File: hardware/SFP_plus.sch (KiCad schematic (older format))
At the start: 20 parts, among them U501 SFPP_CONN

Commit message: Layouted USB-UART.
Also moved USB-OTG to the right Side of the Board. To get there
some free Space, i moved the DDR3/Memory and the FPGA a few
Millimeters down.
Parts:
- R501, R502, R503, R504, R505, R506, R507, R508, R509, R510, R511: footprint Resistors_SMD:R_0402 -> Resistor_SMD:R_0402_1005Metric
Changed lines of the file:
@@
 F 0 "R501" V 6880 3050 50  0000 C CNN
 F 1 "10k" V 6800 3050 50  0000 C CNN
-F 2 "Resistors_SMD:R_0402" V 6730 3050 50  0001 C CNN
+F 2 "Resistor_SMD:R_0402_1005Metric" V 6730 3050 50  0001 C CNN
 F 3 "" H 6800 3050 50  0000 C CNN
 	1    6800 3050
@@
 F 0 "R503" V 7080 3050 50  0000 C CNN
 F 1 "10k" V 7000 3050 50  0000 C CNN
-F 2 "Resistors_SMD:R_0402" V 6930 3050 50  0001 C CNN
+F 2 "Resistor_SMD:R_0402_1005Metric" V 6930 3050 50  0001 C CNN
 F 3 "" H 7000 3050 50  0000 C CNN
 	1    7000 3050
@@
 F 0 "R504" V 7280 3050 50  0000 C CNN
 F 1 "10k" V 7200 3050 50  0000 C CNN
-F 2 "Resistors_SMD:R_0402" V 7130 3050 50  0001 C CNN
+F 2 "Resistor_SMD:R_0402_1005Metric" V 7130 3050 50  0001 C CNN
 F 3 "" H 7200 3050 50  0000 C CNN
 	1    7200 3050
@@
 F 0 "R506" V 7480 3050 50  0000 C CNN
 F 1 "10k" V 7400 3050 50  0000 C CNN
-F 2 "Resistors_SMD:R_0402" V 7330 3050 50  0001 C CNN
+F 2 "Resistor_SMD:R_0402_1005Metric" V 7330 3050 50  0001 C CNN
 F 3 "" H 7400 3050 50  0000 C CNN
 	1    7400 3050
@@
 F 0 "R507" V 7680 3050 50  0000 C CNN
 F 1 "10k" V 7600 3050 50  0000 C CNN
-F 2 "Resistors_SMD:R_0402" V 7530 3050 50  0001 C CNN
+F 2 "Resistor_SMD:R_0402_1005Metric" V 7530 3050 50  0001 C CNN
 F 3 "" H 7600 3050 50  0000 C CNN
 	1    7600 3050
@@
 F 0 "R508" V 7880 3050 50  0000 C CNN
 F 1 "10k" V 7800 3050 50  0000 C CNN
-F 2 "Resistors_SMD:R_0402" V 7730 3050 50  0001 C CNN
+F 2 "Resistor_SMD:R_0402_1005Metric" V 7730 3050 50  0001 C CNN
 F 3 "" H 7800 3050 50  0000 C CNN
 	1    7800 3050
@@
 F 0 "R509" V 8080 3050 50  0000 C CNN
 F 1 "10k" V 8000 3050 50  0000 C CNN
-F 2 "Resistors_SMD:R_0402" V 7930 3050 50  0001 C CNN
+F 2 "Resistor_SMD:R_0402_1005Metric" V 7930 3050 50  0001 C CNN
 F 3 "" H 8000 3050 50  0000 C CNN
 	1    8000 3050
@@
 F 0 "R510" V 8380 3450 50  0000 C CNN
 F 1 "1k" V 8300 3450 50  0000 C CNN
-F 2 "Resistors_SMD:R_0402" V 8230 3450 50  0001 C CNN
+F 2 "Resistor_SMD:R_0402_1005Metric" V 8230 3450 50  0001 C CNN
 F 3 "" H 8300 3450 50  0000 C CNN
 	1    8300 3450
@@
 F 0 "R511" V 8380 3650 50  0000 C CNN
 F 1 "1k" V 8300 3650 50  0000 C CNN
-F 2 "Resistors_SMD:R_0402" V 8230 3650 50  0001 C CNN
+F 2 "Resistor_SMD:R_0402_1005Metric" V 8230 3650 50  0001 C CNN
 F 3 "" H 8300 3650 50  0000 C CNN
 	1    8300 3650
@@
 F 0 "R502" V 6880 4450 50  0000 C CNN
 F 1 "DNP" V 6800 4450 50  0000 C CNN
-F 2 "Resistors_SMD:R_0402" V 6730 4450 50  0001 C CNN
+F 2 "Resistor_SMD:R_0402_1005Metric" V 6730 4450 50  0001 C CNN
 F 3 "" H 6800 4450 50  0000 C CNN
 	1    6800 4450
@@
 F 0 "R505" V 7280 4450 50  0000 C CNN
 F 1 "DNP" V 7200 4450 50  0000 C CNN
-F 2 "Resistors_SMD:R_0402" V 7130 4450 50  0001 C CNN
+F 2 "Resistor_SMD:R_0402_1005Metric" V 7130 4450 50  0001 C CNN
 F 3 "" H 7200 4450 50  0000 C CNN
 	1    7200 4450

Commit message: Improved Powerdistribution Network of the FPGA.
Also started to layout USB.
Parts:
- C501, C502, C503, C504, C505, C506: footprint Capacitors_SMD:C_0402 -> Capacitor_SMD:C_0402_1005Metric
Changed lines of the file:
@@
 F 0 "C505" H 3325 3550 50  0000 L CNN
 F 1 "0.1uF" H 3325 3350 50  0000 L CNN
-F 2 "Capacitors_SMD:C_0402" H 3338 3300 50  0001 C CNN
+F 2 "Capacitor_SMD:C_0402_1005Metric" H 3338 3300 50  0001 C CNN
 F 3 "" H 3300 3450 50  0000 C CNN
 	1    3300 3450
@@
 F 0 "C503" H 3025 3550 50  0000 L CNN
 F 1 "22uF" H 3025 3350 50  0000 L CNN
-F 2 "Capacitors_SMD:C_0402" H 3038 3300 50  0001 C CNN
+F 2 "Capacitor_SMD:C_0402_1005Metric" H 3038 3300 50  0001 C CNN
 F 3 "" H 3000 3450 50  0000 C CNN
 	1    3000 3450
@@
 F 0 "C501" H 2325 3550 50  0000 L CNN
 F 1 "0.1uF" H 2325 3350 50  0000 L CNN
-F 2 "Capacitors_SMD:C_0402" H 2338 3300 50  0001 C CNN
+F 2 "Capacitor_SMD:C_0402_1005Metric" H 2338 3300 50  0001 C CNN
 F 3 "" H 2300 3450 50  0000 C CNN
 	1    2300 3450
@@
 F 0 "C506" H 3325 4450 50  0000 L CNN
 F 1 "0.1uF" H 3325 4250 50  0000 L CNN
-F 2 "Capacitors_SMD:C_0402" H 3338 4200 50  0001 C CNN
+F 2 "Capacitor_SMD:C_0402_1005Metric" H 3338 4200 50  0001 C CNN
 F 3 "" H 3300 4350 50  0000 C CNN
 	1    3300 4350
@@
 F 0 "C504" H 3025 4450 50  0000 L CNN
 F 1 "22uF" H 3025 4250 50  0000 L CNN
-F 2 "Capacitors_SMD:C_0402" H 3038 4200 50  0001 C CNN
+F 2 "Capacitor_SMD:C_0402_1005Metric" H 3038 4200 50  0001 C CNN
 F 3 "" H 3000 4350 50  0000 C CNN
 	1    3000 4350
@@
 F 0 "C502" H 2325 4450 50  0000 L CNN
 F 1 "0.1uF" H 2325 4250 50  0000 L CNN
-F 2 "Capacitors_SMD:C_0402" H 2338 4200 50  0001 C CNN
+F 2 "Capacitor_SMD:C_0402_1005Metric" H 2338 4200 50  0001 C CNN
 F 3 "" H 2300 4350 50  0000 C CNN
 	1    2300 4350

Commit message: Fixed Schematic Symbols
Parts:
- C501, C502, C503, C504, C505, C506: symbol device:C -> Device:C_Small
- L501, L502: symbol device:L_Small -> Device:L_Small
- R501, R502, R503, R504, R505, R506, R507, R508, R509, R510, R511: symbol device:R -> Device:R
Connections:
- wire segments 85 -> 91
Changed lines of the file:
@@
 $Descr A4 11693 8268
 encoding utf-8
-Sheet 5 22
+Sheet 5 21
 Title ""
 Date ""
@@
 $EndComp
 $Comp
-L device:C C505
+L Device:C_Small C505
 U 1 1 5973C515
 P 3300 3450
@@
 $EndComp
 $Comp
-L device:C C503
+L Device:C_Small C503
 U 1 1 5973C862
 P 3000 3450
@@
 $EndComp
 $Comp
-L device:C C501
+L Device:C_Small C501
 U 1 1 5973C883
 P 2300 3450
@@
 $EndComp
 $Comp
-L device:C C506
+L Device:C_Small C506
 U 1 1 5973C8C6
 P 3300 4350
@@
 $EndComp
 $Comp
-L device:C C504
+L Device:C_Small C504
 U 1 1 5973C8FD
 P 3000 4350
@@
 $EndComp
 $Comp
-L device:C C502
+L Device:C_Small C502
 U 1 1 5973C92A
 P 2300 4350
@@
 $EndComp
 $Comp
-L device:L_Small L501
+L Device:L_Small L501
 U 1 1 5973CA0B
 P 2650 3200
@@
 $EndComp
 $Comp
-L device:L_Small L502
+L Device:L_Small L502
 U 1 1 5973CA4A
 P 2650 4100
@@
 $EndComp
 Wire Wire Line
-	3300 3300 3300 3200
-Wire Wire Line
 	2750 3200 3000 3200
-Wire Wire Line
-	3000 3300 3000 3200
 Connection ~ 3000 3200
 Wire Wire Line
@@
 	2300 4100 2550 4100
 Wire Wire Line
-	3000 4200 3000 4100
-Wire Wire Line
 	2750 4100 3000 4100
-Wire Wire Line
-	3300 4200 3300 4100
 Connection ~ 3000 4100
 $Comp
-L power1:+3V3 #PWR026
+L power:+3V3 #PWR026
 U 1 1 5973CBAF
 P 2300 3150
@@
 $EndComp
 $Comp
-L power1:+3V3 #PWR027
+L power:+3V3 #PWR027
 U 1 1 5973CBD5
 P 2300 4050
@@
 Connection ~ 2300 4100
 $Comp
-L power1:GND #PWR028
+L power:GND #PWR028
 U 1 1 5973CC3E
 P 3300 3600
@@
 $EndComp
 $Comp
-L power1:GND #PWR029
+L power:GND #PWR029
 U 1 1 5973CC64
 P 3000 3600
@@
 $EndComp
 $Comp
-L power1:GND #PWR030
+L power:GND #PWR030
 U 1 1 5973CD98
 P 2300 3600
@@
 $EndComp
 $Comp
-L power1:GND #PWR031
+L power:GND #PWR031
 U 1 1 5973CDD0
 P 3300 4500
@@
 $EndComp
 $Comp
-L power1:GND #PWR032
+L power:GND #PWR032
 U 1 1 5973CDF6
 P 3000 4500
@@
 $EndComp
 $Comp
-L power1:GND #PWR033
+L power:GND #PWR033
 U 1 1 5973CE1C
 P 2300 4500
@@
 Connection ~ 3300 4100
 $Comp
-L power1:GND #PWR034
+L power:GND #PWR034
 U 1 1 5973DD7C
 P 4500 4500
@@
 Connection ~ 6450 4300
 $Comp
-L power1:GND #PWR035
+L power:GND #PWR035
 U 1 1 5973DEDC
 P 6450 4500
@@
 $EndComp
 $Comp
-L device:R R501
+L Device:R R501
 U 1 1 5973DF65
 P 6800 3050
@@
 $EndComp
 $Comp
-L device:R R503
+L Device:R R503
 U 1 1 5973DF9C
 P 7000 3050
@@
 $EndComp
 $Comp
-L device:R R504
+L Device:R R504
 U 1 1 5973DFC7
 P 7200 3050
@@
 $EndComp
 $Comp
-L device:R R506
+L Device:R R506
 U 1 1 5973DFF4
 P 7400 3050
@@
 $EndComp
 $Comp
-L device:R R507
+L Device:R R507
 U 1 1 5973E023
 P 7600 3050
@@
 $EndComp
 $Comp
-L device:R R508
+L Device:R R508
 U 1 1 5973E070
 P 7800 3050
@@
 $EndComp
 $Comp
-L device:R R509
+L Device:R R509
 U 1 1 5973E0A7
 P 8000 3050
@@
 Connection ~ 7800 2800
 $Comp
-L power1:+3V3 #PWR036
+L power:+3V3 #PWR036
 U 1 1 5973E37C
 P 7400 2700
@@
 	8000 4200 8000 3200
 $Comp
-L device:R R510
+L Device:R R510
 U 1 1 5973E623
 P 8300 3450
@@
 $EndComp
 $Comp
-L device:R R511
+L Device:R R511
 U 1 1 5973E65E
 P 8300 3650
@@
 SFP_GPIO
 $Comp
-L device:R R502
+L Device:R R502
 U 1 1 5973F1E4
 P 6800 4450
@@
 $EndComp
 $Comp
-L device:R R505
+L Device:R R505
 U 1 1 5973F225
 P 7200 4450
@@
 $EndComp
 $Comp
-L power1:GND #PWR037
+L power:GND #PWR037
 U 1 1 5973F2EE
 P 7000 4700
@@
 	3000 4100 3300 4100
 Wire Wire Line
-	2300 3200 2300 3300
-Wire Wire Line
-	2300 4100 2300 4200
-Wire Wire Line
 	4500 4350 4500 4500
 Wire Wire Line
@@
 Wire Wire Line
 	3300 3200 3600 3200
+Wire Wire Line
+	2300 4450 2300 4500
+Wire Wire Line
+	3000 4500 3000 4450
+Wire Wire Line
+	3300 4450 3300 4500
+Wire Wire Line
+	3300 4100 3300 4250
+Wire Wire Line
+	3000 4100 3000 4250
+Wire Wire Line
+	2300 4100 2300 4250
+Wire Wire Line
+	2300 3550 2300 3600
+Wire Wire Line
+	3000 3600 3000 3550
+Wire Wire Line
+	3300 3550 3300 3600
+Wire Wire Line
+	3300 3200 3300 3350
+Wire Wire Line
+	3000 3200 3000 3350
+Wire Wire Line
+	2300 3200 2300 3350
 $EndSCHEMATC

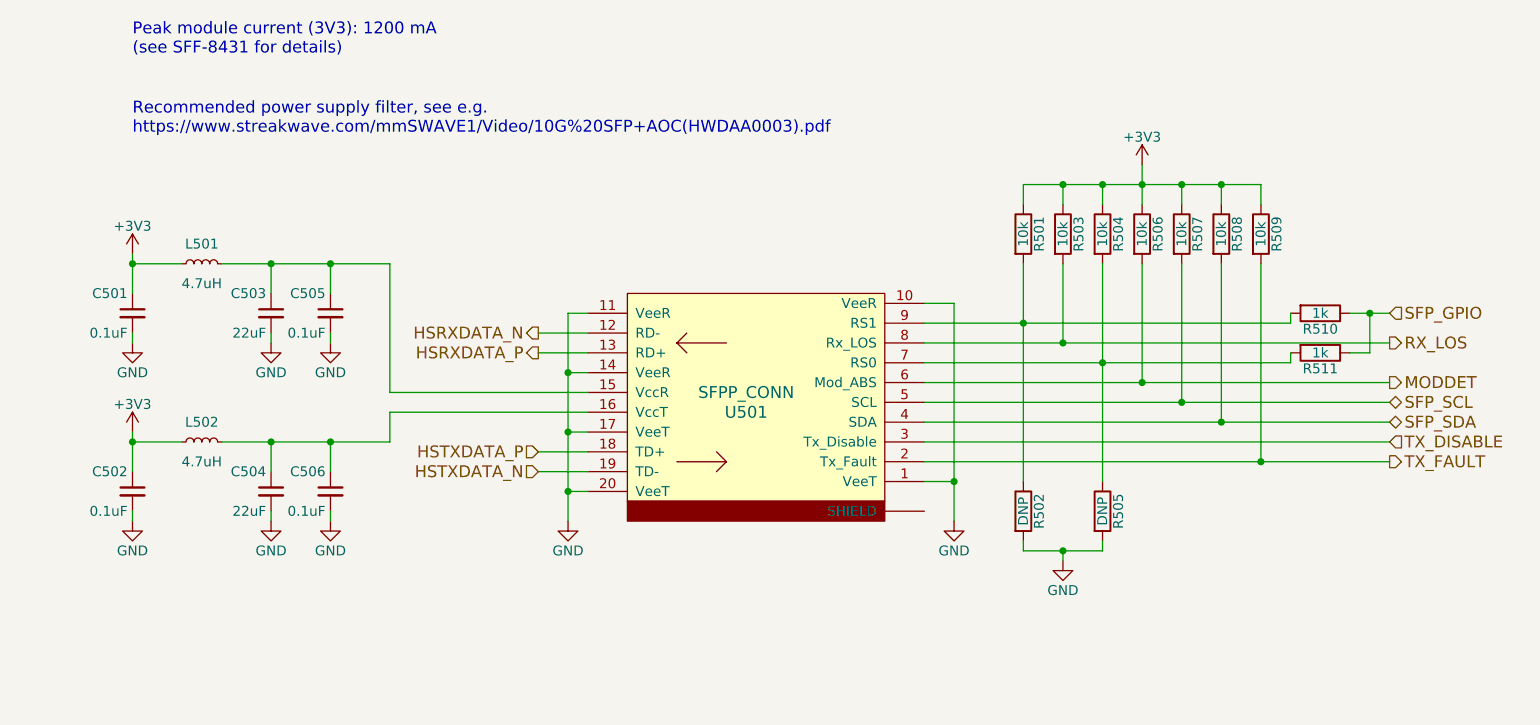
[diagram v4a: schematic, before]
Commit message: SFP+ Power Filter, Levelshifter and MGT/TLK Clock Distribution.
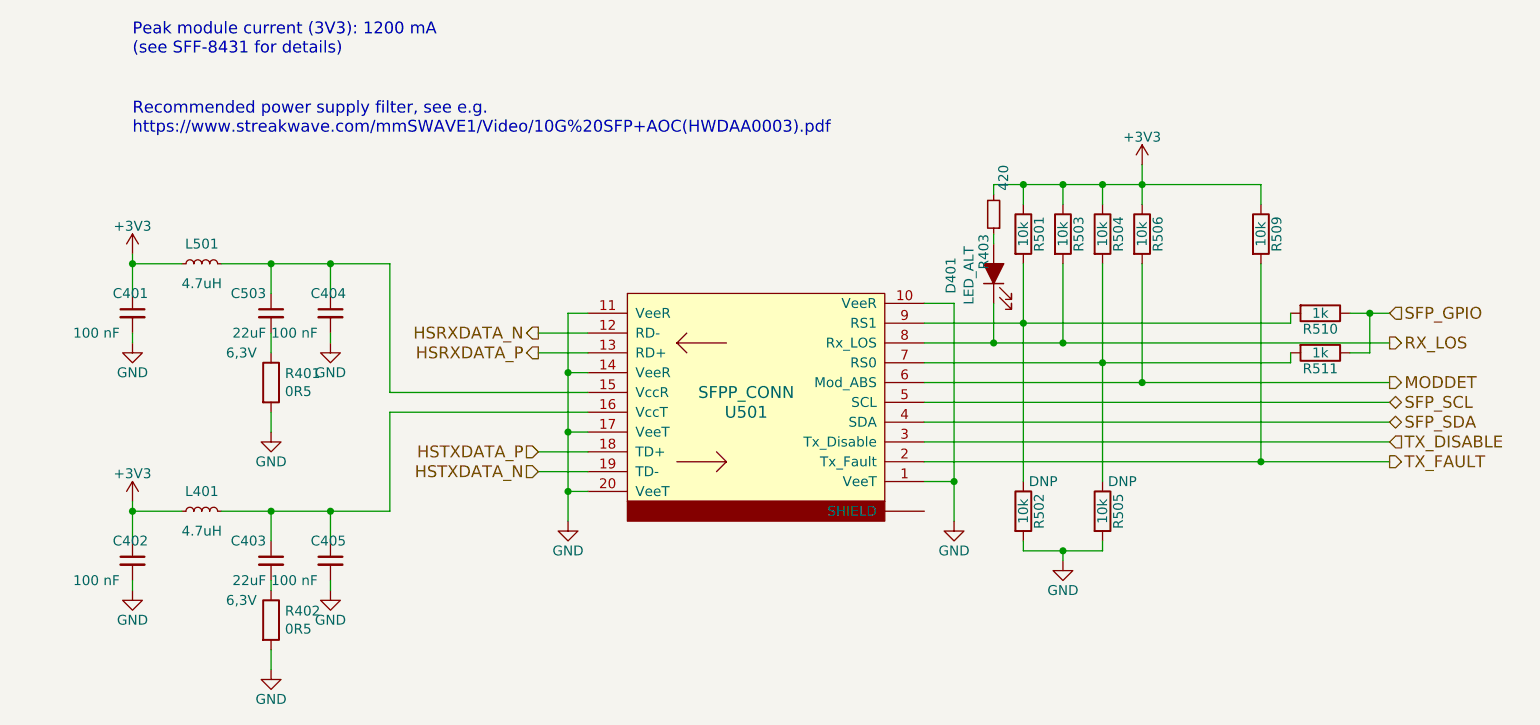
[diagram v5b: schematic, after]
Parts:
- removed C501, C502, C505, C506: 0.1uF, Capacitor_SMD:C_0402_1005Metric, symbol Device:C_Small
- removed C504: 22uF, Capacitor_SMD:C_0402_1005Metric, symbol Device:C_Small
- removed L502: 4.7uH, symbol Device:L_Small
- removed R507, R508: 10k, Resistor_SMD:R_0402_1005Metric, symbol Device:R
- added C401, C402, C404, C405: 100 nF, Capacitor_SMD:C_0201_0603Metric, symbol Device:C_Small
- added C403: 22uF, Capacitor_SMD:C_0603_1608Metric, symbol Device:C_Small
- added D401: LED_ALT, LED_SMD:LED_0603_1608Metric, symbol Device:LED_ALT
- added L401: 4.7uH, Inductor_SMD:L_1210_3225Metric, symbol Device:L_Small
- added R401, R402: 0R5, Resistor_SMD:R_0603_1608Metric, symbol Device:R
- added R403: 420, Resistor_SMD:R_0402_1005Metric, symbol Device:R_Small
- C503: footprint Capacitor_SMD:C_0402_1005Metric -> Capacitor_SMD:C_0603_1608Metric; Description (none) -> CAP CER 22UF 6.3V X5R 0603; Digikey (none) -> 490-13241-1-ND; MFG Name (none) -> Murata Electronics North America; MFG Part Num (none) -> GRM186R60J226ME15D; Populate for CLG484(Z-7012s/Z-7015) (none) -> 1; Populate for SBGA485(Z-7030) (none) -> 1; Populated (none) -> 1; Source (none) -> SPEC; Voltage (none) -> 6,3V
- L501: footprint (none) -> Inductor_SMD:L_1210_3225Metric; Description (none) -> FIXED IND 4.7UH 1.01A 130 MOHM; Digikey (none) -> 587-1624-1-ND; MFG Name (none) -> Taiyo Yuden; MFG Part Num (none) -> CBC3225T4R7MR; Populate for CLG484(Z-7012s/Z-7015) (none) -> 1; Populate for SBGA485(Z-7030) (none) -> 1; Populated (none) -> 1; Source (none) -> SPEC
- R502, R505: value DNP -> 10k; Populate for CLG484(Z-7012s/Z-7015) (none) -> 1; Populate for SBGA485(Z-7030) (none) -> 1; Populated (none) -> DNP; Source (none) -> SPEC
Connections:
- net +3V3: now also C401.1, C402.1, L401.2, R403.2
- net GND: now also C401.2, C402.2, C404.2, C405.2, R401.2, R402.2; no longer C503.2
- net RX_LOS: now also D401.1 (K)
- net at C503.1, L501.1, U501.15 (VccR): now also C404.1
- net at U501.16 (VccT): now also C403.1, C405.1, L401.1
- new net: C503.2, R401.1
- new net: C403.2, R402.1
- new net: D401.2 (A), R403.1

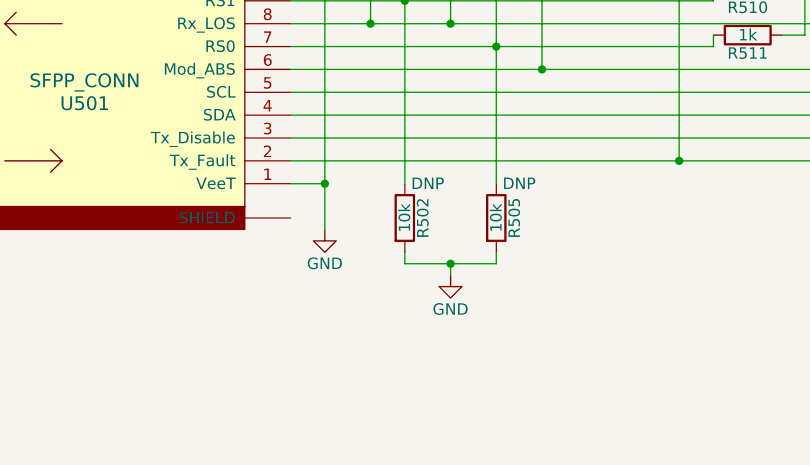
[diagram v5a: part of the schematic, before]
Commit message: PS Clock, Reset Button, Cam Levelshifters and big 1.0 V Cap placed.
Improved some Footprints and library Symbols.

Also though about Chassis Ground.
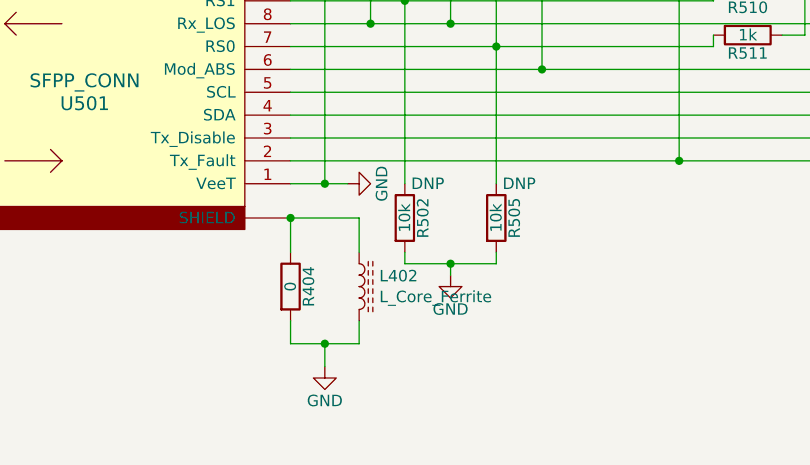
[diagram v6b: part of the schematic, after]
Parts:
- added L402: L_Core_Ferrite, Inductor_SMD:L_0805_2012Metric, symbol Device:L_Core_Ferrite
- added R404: 0, Resistor_SMD:R_0402_1005Metric, symbol Device:R
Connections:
- net GND: now also L402.2, R404.2
- net at U501.SHIELD: now also L402.1, R404.1
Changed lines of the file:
@@
 L power:GND #PWR035
 U 1 1 5973DEDC
-P 6450 4500
-F 0 "#PWR035" H 6450 4250 50  0001 C CNN
-F 1 "GND" H 6450 4350 50  0000 C CNN
-F 2 "" H 6450 4500 50  0000 C CNN
-F 3 "" H 6450 4500 50  0000 C CNN
-	1    6450 4500
-	1    0    0    -1
+P 6550 4300
+F 0 "#PWR035" H 6550 4050 50  0001 C CNN
+F 1 "GND" H 6550 4150 50  0000 C CNN
+F 2 "" H 6550 4300 50  0000 C CNN
+F 3 "" H 6550 4300 50  0000 C CNN
+	1    6550 4300
+	0    -1   -1   0
 $EndComp
 $Comp
@@
 	3300 4450 3600 4450
 Wire Wire Line
-	6450 4300 6450 4500
+	6450 4300 6550 4300
 Wire Wire Line
 	7000 2800 7200 2800
@@
 Wire Wire Line
 	7400 2800 8000 2800
+$Comp
+L Device:R R404
+U 1 1 5BBF0B26
+P 6300 4750
+F 0 "R404" V 6380 4750 50  0000 C CNN
+F 1 "0" V 6300 4750 50  0000 C CNN
+F 2 "Resistor_SMD:R_0402_1005Metric" V 6230 4750 50  0001 C CNN
+F 3 "" H 6300 4750 50  0000 C CNN
+F 4 "1" H 6400 4900 50  0001 C CNN "Populated"
+F 5 "SPEC" H 6300 4750 50  0001 C CNN "Source"
+F 6 "1" H 6300 4750 50  0001 C CNN "Populate for SBGA485(Z-7030)"
+F 7 "1" H 6300 4750 50  0001 C CNN "Populate for CLG484(Z-7012s/Z-7015)"
+	1    6300 4750
+	1    0    0    -1
+$EndComp
+Wire Wire Line
+	6300 4450 6300 4600
+Wire Wire Line
+	6300 4450 6600 4450
+Wire Wire Line
+	6600 4450 6600 4600
+Connection ~ 6300 4450
+Wire Wire Line
+	6300 4900 6300 5000
+Wire Wire Line
+	6300 5000 6450 5000
+Wire Wire Line
+	6600 5000 6600 4900
+$Comp
+L power:GND #PWR0401
+U 1 1 5BBF7A87
+P 6450 5100
+F 0 "#PWR0401" H 6450 4850 50  0001 C CNN
+F 1 "GND" H 6450 4950 50  0000 C CNN
+F 2 "" H 6450 5100 50  0000 C CNN
+F 3 "" H 6450 5100 50  0000 C CNN
+	1    6450 5100
+	1    0    0    -1
+$EndComp
+Wire Wire Line
+	6450 5100 6450 5000
+Connection ~ 6450 5000
+Wire Wire Line
+	6450 5000 6600 5000
+$Comp
+L Device:L_Core_Ferrite L402
+U 1 1 5BC02334
+P 6600 4750
+F 0 "L402" H 6688 4796 50  0000 L CNN
+F 1 "L_Core_Ferrite" H 6688 4705 50  0000 L CNN
+F 2 "Inductor_SMD:L_0805_2012Metric" H 6600 4750 50  0001 C CNN
+F 3 "~" H 6600 4750 50  0001 C CNN
+F 4 "1" H 6600 4750 50  0001 C CNN "Populated"
+F 5 "SPEC" H 6600 4750 50  0001 C CNN "Source"
+F 6 "1" H 6600 4750 50  0001 C CNN "Populate for SBGA485(Z-7030)"
+F 7 "1" H 6600 4750 50  0001 C CNN "Populate for CLG484(Z-7012s/Z-7015)"
+	1    6600 4750
+	1    0    0    -1
+$EndComp
 $EndSCHEMATC

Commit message: WIP: routing the HF Part of the Camera Connector. I have to move the clock away from the left border.
TODO: Fix DDR3 RAM.
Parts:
- added PO401, PO402: POWER_OUTPUT, footprints:EMPTY, symbol fixme:POWER_OUTPUT
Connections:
- wire segments 98 -> 100
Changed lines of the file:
@@
 $EndComp
 Wire Wire Line
-	2750 3200 3000 3200
+	2750 3200 2800 3200
 Connection ~ 3000 3200
 Wire Wire Line
@@
 	2300 4450 2550 4450
 Wire Wire Line
-	2750 4450 3000 4450
+	2750 4450 2800 4450
 Connection ~ 3000 4450
 $Comp
@@
 	1    0    0    -1
 $EndComp
+$Comp
+L fixme:POWER_OUTPUT PO401
+U 1 1 5BEC3DBF
+P 2800 3100
+F 0 "PO401" H 2800 3100 50  0001 C CNN
+F 1 "POWER_OUTPUT" H 2800 3250 50  0001 C CNN
+F 2 "footprints:EMPTY" H 2800 3100 50  0001 C CNN
+F 3 "" H 2800 3100 50  0001 C CNN
+	1    2800 3100
+	1    0    0    -1
+$EndComp
+Connection ~ 2800 3200
+Wire Wire Line
+	2800 3200 3000 3200
+$Comp
+L fixme:POWER_OUTPUT PO402
+U 1 1 5BEC3F5D
+P 2800 4350
+F 0 "PO402" H 2800 4350 50  0001 C CNN
+F 1 "POWER_OUTPUT" H 2800 4500 50  0001 C CNN
+F 2 "footprints:EMPTY" H 2800 4350 50  0001 C CNN
+F 3 "" H 2800 4350 50  0001 C CNN
+	1    2800 4350
+	1    0    0    -1
+$EndComp
+Connection ~ 2800 4450
+Wire Wire Line
+	2800 4450 3000 4450
 $EndSCHEMATC
